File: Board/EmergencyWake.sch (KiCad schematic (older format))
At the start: 129 parts, among them J1 USB_C_Receptacle_USB2.0, J2 Micro_SD_Card_Det, J3 Conn_01x03, J4 Conn_01x02, J5 Conn_01x03, J6 Conn_01x04, J7 Conn_01x02, J8 Conn_01x04, J9 Conn_01x04, Q1 AO3400A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

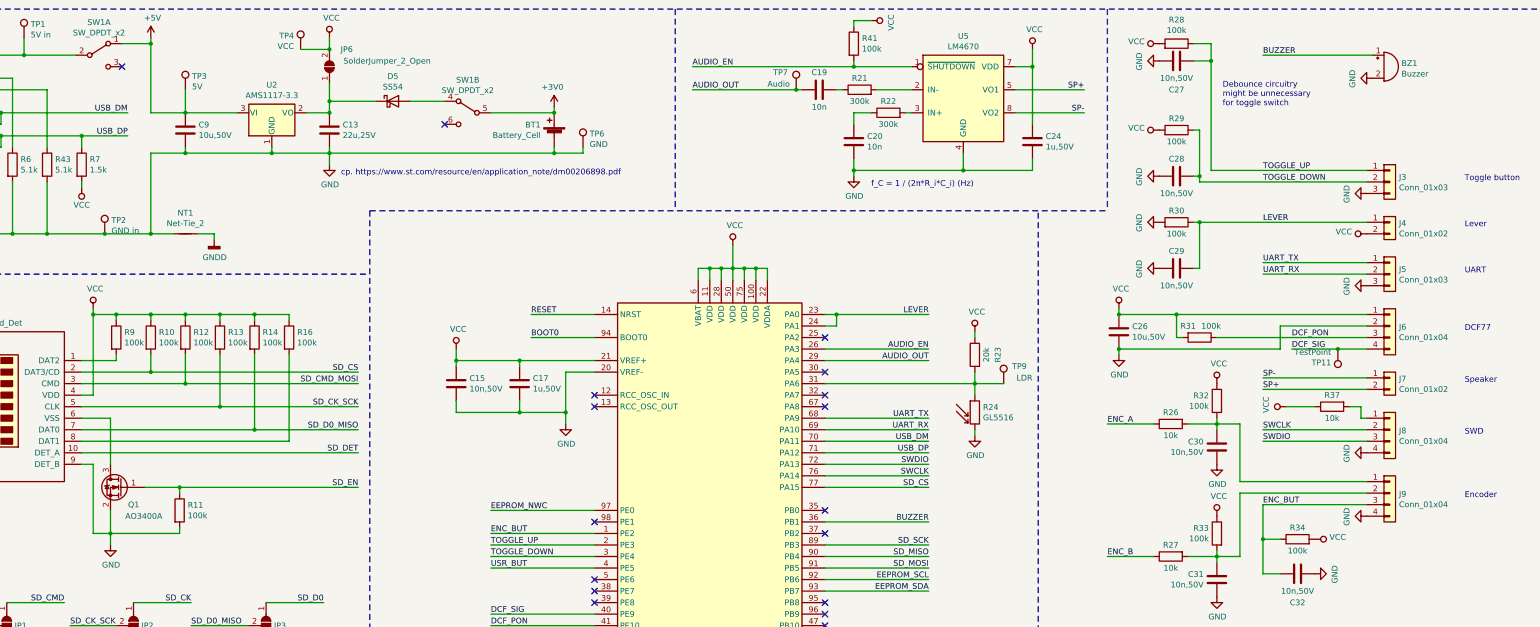
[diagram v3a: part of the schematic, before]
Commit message: [Board] Changed SD and battery holder to Würth components
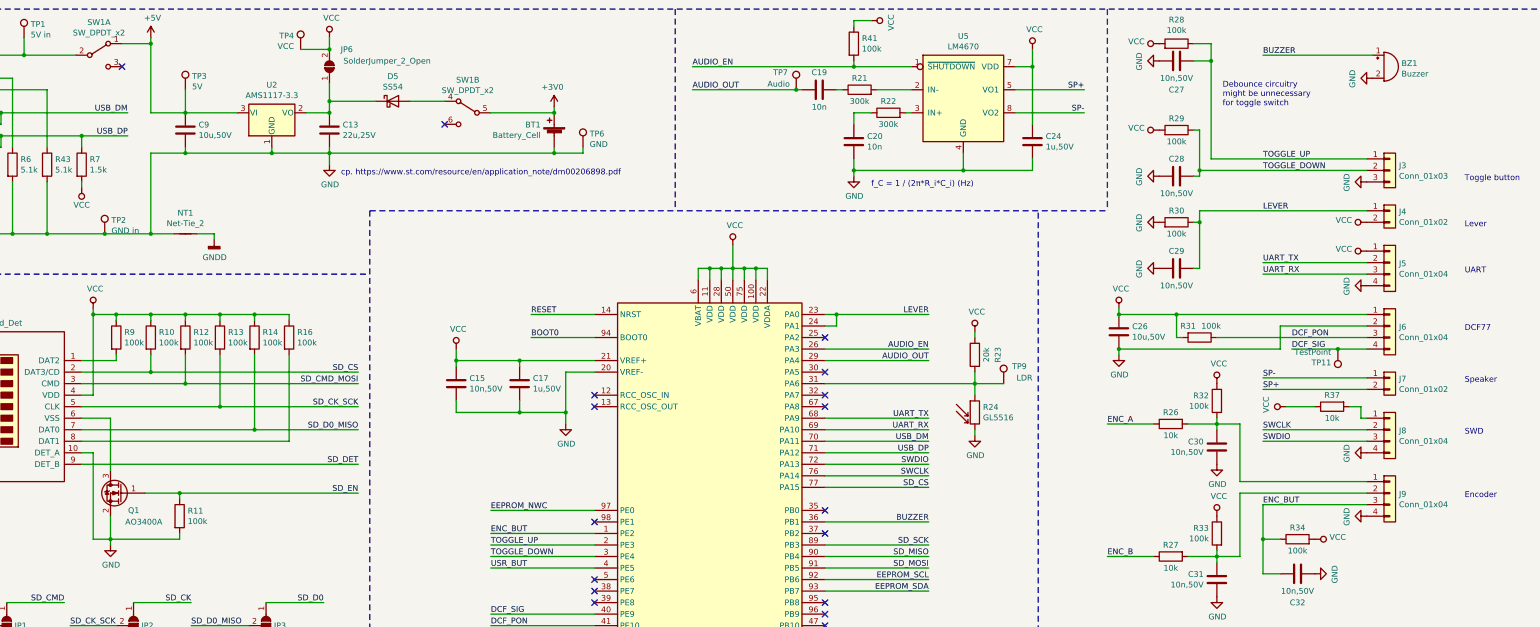
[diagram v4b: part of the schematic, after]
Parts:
- removed J5: Conn_01x03, Connector_PinHeader_2.54mm:PinHeader_1x03_P2.54mm_Horizontal, symbol Connector_Generic:Conn_01x03
- added J5: Conn_01x04, Connector_PinHeader_2.54mm:PinHeader_1x04_P2.54mm_Horizontal, symbol Connector_Generic:Conn_01x04
- BT1: footprint Battery:BatteryHolder_Keystone_3002_1x2032 -> Wuerth:79523141; Conrad 1009388 - 62 -> (none); Würth (none) -> 79523141
- J1: Würth (none) -> 632723300011
- J2: footprint Card:microSD_Attend_112I-TDAR-R 1 -> Wuerth:693071020811; Conrad 1308329 - 62 -> (none); Würth (none) -> 693071020811
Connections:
- net GND: now also J2.10 (DET_A), J5.4 (Pin_4); no longer J2.9 (DET_B)
- net SD_DET: now also J2.9 (DET_B); no longer J2.10 (DET_A)
- net UART_RX: now also J5.3 (Pin_3)
- net UART_TX: now also J5.2 (Pin_2)
- net VCC: now also J5.1 (Pin_1)
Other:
- moved on the sheet: J3, J4, Q1, R11
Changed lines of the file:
@@
 L Connector_Generic:Conn_01x02 J4
 U 1 1 5E2B13EE
-P 13900 2400
-F 0 "J4" H 13980 2392 50  0000 L CNN
-F 1 "Conn_01x02" H 13980 2301 50  0000 L CNN
-F 2 "Connector_PinHeader_2.54mm:PinHeader_1x02_P2.54mm_Horizontal" H 13900 2400 50  0001 C CNN
-F 3 "~" H 13900 2400 50  0001 C CNN
-	1    13900 2400
+P 13900 2300
+F 0 "J4" H 13980 2292 50  0000 L CNN
+F 1 "Conn_01x02" H 13980 2201 50  0000 L CNN
+F 2 "Connector_PinHeader_2.54mm:PinHeader_1x02_P2.54mm_Horizontal" H 13900 2300 50  0001 C CNN
+F 3 "~" H 13900 2300 50  0001 C CNN
+	1    13900 2300
 	1    0    0    -1
 $EndComp
@@
 F 0 "J2" H 1600 4817 50  0000 C CNN
 F 1 "Micro_SD_Card_Det" H 1600 4726 50  0000 C CNN
-F 2 "Card:microSD_Attend_112I-TDAR-R 1" H 3700 4700 50  0001 C CNN
-F 3 "https://asset.conrad.com/media10/add/160267/c1/-/en/001308329DS01/datenblatt-1308329-attend-microsd-kartensockel-druck-druck-112i-tdar-r-1-st.pdf" H 1650 4100 50  0001 C CNN
-F 4 "1308329 - 62" H 1650 4000 50  0001 C CNN "Conrad"
+F 2 "Wuerth:693071020811" H 3700 4700 50  0001 C CNN
+F 3 "https://www.we-online.de/katalog/datasheet/693071020811.pdf" H 1650 4100 50  0001 C CNN
+F 4 "693071020811" H 1650 4000 50  0001 C CNN "Würth"
 	1    1650 4000
 	-1   0    0    -1
@@
 F 0 "BT1" H 6768 1746 50  0000 L CNN
 F 1 "Battery_Cell" H 6768 1655 50  0000 L CNN
-F 2 "Battery:BatteryHolder_Keystone_3002_1x2032" V 6650 1710 50  0001 C CNN
-F 3 "https://www.conrad.de/de/p/renata-100340-knopfzellenhalter-1x-cr-2032-horizontal-oberflaechenmontage-smd-l-x-b-x-h-30-7-x-20-x-4-mm-1009388.html" V 6650 1710 50  0001 C CNN
-F 4 "1009388 - 62" H 6650 1650 50  0001 C CNN "Conrad"
+F 2 "Wuerth:79523141" V 6650 1710 50  0001 C CNN
+F 3 "https://www.we-online.de/katalog/datasheet/79523141.pdf" V 6650 1710 50  0001 C CNN
+F 4 "79523141" H 6650 1650 50  0001 C CNN "Würth"
 	1    6650 1650
 	-1   0    0    -1
@@
 	6650 1450 6100 1450
 Connection ~ 6650 1450
-$Comp
-L Connector_Generic:Conn_01x03 J5
-U 1 1 5E2E2ED5
-P 13900 2850
-F 0 "J5" H 13980 2892 50  0000 L CNN
-F 1 "Conn_01x03" H 13980 2801 50  0000 L CNN
-F 2 "Connector_PinHeader_2.54mm:PinHeader_1x03_P2.54mm_Horizontal" H 13900 2850 50  0001 C CNN
-F 3 "~" H 13900 2850 50  0001 C CNN
-	1    13900 2850
-	1    0    0    -1
-$EndComp
 Text Notes 14550 2850 0    50   ~ 0
 UART
@@
 L Device:Q_NMOS_GSD Q1
 U 1 1 5E31A1D8
-P 2900 4700
-F 0 "Q1" H 2750 4550 50  0000 L CNN
-F 1 "AO3400A" H 2550 4450 50  0000 L CNN
-F 2 "Package_TO_SOT_SMD:SOT-23" H 3100 4800 50  0001 C CNN
-F 3 "https://datasheet.lcsc.com/szlcsc/Alpha-Omega-Semicon-AOS-AO3400A_C20917.pdf" H 2900 4700 50  0001 C CNN
-F 4 "C20917" H 2900 4700 50  0001 C CNN "LCSC"
-	1    2900 4700
+P 2900 4750
+F 0 "Q1" H 2750 4600 50  0000 L CNN
+F 1 "AO3400A" H 2550 4500 50  0000 L CNN
+F 2 "Package_TO_SOT_SMD:SOT-23" H 3100 4850 50  0001 C CNN
+F 3 "https://datasheet.lcsc.com/szlcsc/Alpha-Omega-Semicon-AOS-AO3400A_C20917.pdf" H 2900 4750 50  0001 C CNN
+F 4 "C20917" H 2900 4750 50  0001 C CNN "LCSC"
+	1    2900 4750
 	-1   0    0    -1
 $EndComp
@@
 	2550 4100 2800 4100
 Wire Wire Line
-	2800 4100 2800 4500
+	2800 4100 2800 4550
 Wire Wire Line
-	2800 4900 2800 5100
+	2800 4950 2800 5150
 Wire Wire Line
-	2650 5100 2800 5100
-Connection ~ 2800 5100
+	2650 5150 2800 5150
+Connection ~ 2800 5150
 Wire Wire Line
-	2800 5100 2800 5200
+	2800 5150 2800 5200
 Wire Wire Line
 	2550 3900 2650 3900
@@
 $EndComp
 Wire Wire Line
-	3100 4700 3400 4700
+	3100 4750 3400 4750
 $Comp
 L power:GND #PWR03
@@
 $EndComp
 Wire Wire Line
-	2800 5100 3400 5100
+	2800 5150 3400 5150
 Wire Wire Line
-	3400 5100 3400 5050
+	3400 5150 3400 5100
 Wire Wire Line
-	3400 4750 3400 4700
-Connection ~ 3400 4700
+	3400 4800 3400 4750
+Connection ~ 3400 4750
 Wire Wire Line
-	3400 4700 4950 4700
-Text Label 4950 4700 2    50   ~ 0
+	3400 4750 4950 4750
+Text Label 4950 4750 2    50   ~ 0
 SD_EN
-Text Label 4950 4400 2    50   ~ 0
+Text Label 4950 4500 2    50   ~ 0
 SD_DET
 $Comp
@@
 L Device:R R11
 U 1 1 5E33508E
-P 3400 4900
-F 0 "R11" H 3470 4946 50  0000 L CNN
-F 1 "100k" H 3470 4855 50  0000 L CNN
-F 2 "Resistor_SMD:R_0402_1005Metric" V 3330 4900 50  0001 C CNN
-F 3 "~" H 3400 4900 50  0001 C CNN
-F 4 "C25741" H 3400 4900 50  0001 C CNN "LCSC"
-	1    3400 4900
+P 3400 4950
+F 0 "R11" H 3470 4996 50  0000 L CNN
+F 1 "100k" H 3470 4905 50  0000 L CNN
+F 2 "Resistor_SMD:R_0402_1005Metric" V 3330 4950 50  0001 C CNN
+F 3 "~" H 3400 4950 50  0001 C CNN
+F 4 "C25741" H 3400 4950 50  0001 C CNN "LCSC"
+	1    3400 4950
 	1    0    0    -1
 $EndComp
@@
 Text Label 13050 3500 0    50   ~ 0
 DCF_SIG
-Text Label 12800 1950 0    50   ~ 0
+Text Label 12800 1850 0    50   ~ 0
 TOGGLE_UP
-Text Label 12800 2050 0    50   ~ 0
+Text Label 12800 1950 0    50   ~ 0
 TOGGLE_DOWN
-Text Label 12800 2400 0    50   ~ 0
+Text Label 12800 2300 0    50   ~ 0
 LEVER
 Text Label 11450 4150 0    50   ~ 0
@@
 $EndComp
 Wire Wire Line
-	12200 2400 12250 2400
-Wire Wire Line
 	12200 2800 12250 2800
 Wire Wire Line
 	12250 2800 12250 2400
-Connection ~ 12250 2400
 Wire Wire Line
-	12250 2400 13700 2400
+	12250 2300 13700 2300
 Wire Wire Line
-	12250 2050 12250 2000
+	12250 1950 12250 2000
 Wire Wire Line
 	12250 2000 12200 2000
@@
 	12200 1600 12250 1600
 Wire Wire Line
-	12250 1600 12250 2000
-Connection ~ 12250 2000
+	12250 1600 12250 1950
 Wire Wire Line
-	12350 1950 12350 1000
+	12350 1850 12350 1000
 Wire Wire Line
 	12350 1000 12200 1000
@@
 $EndComp
 $Comp
-L Connector:TestPoint TP1
-U 1 1 5E3C768F
-P 2050 800
-F 0 "TP1" H 2108 918 50  0000 L CNN
-F 1 "5V in" H 2108 827 50  0000 L CNN
-F 2 "TestPoint:TestPoint_Loop_D1.80mm_Drill1.0mm_Beaded" H 2250 800 50  0001 C CNN
-F 3 "~" H 2250 800 50  0001 C CNN
-	1    2050 800
-	1    0    0    -1
-$EndComp
-$Comp
 L Connector:TestPoint TP2
 U 1 1 5E3C8161
@@
 	5050 2300 11450 2300
 Wire Wire Line
-	12250 2050 13700 2050
+	12250 1950 13700 1950
 Wire Wire Line
-	12350 1950 13700 1950
+	12350 1850 13700 1850
 $Comp
 L Connector_Generic:Conn_01x03 J3
 U 1 1 5E2B1093
-P 13900 2050
-F 0 "J3" H 13980 2092 50  0000 L CNN
-F 1 "Conn_01x03" H 13980 2001 50  0000 L CNN
-F 2 "Connector_PinHeader_2.54mm:PinHeader_1x03_P2.54mm_Horizontal" H 13900 2050 50  0001 C CNN
-F 3 "~" H 13900 2050 50  0001 C CNN
-	1    13900 2050
+P 13900 1950
+F 0 "J3" H 13980 1992 50  0000 L CNN
+F 1 "Conn_01x03" H 13980 1901 50  0000 L CNN
+F 2 "Connector_PinHeader_2.54mm:PinHeader_1x03_P2.54mm_Horizontal" H 13900 1950 50  0001 C CNN
+F 3 "~" H 13900 1950 50  0001 C CNN
+	1    13900 1950
 	1    0    0    -1
 $EndComp
@@
 L power:VCC #PWR048
 U 1 1 5E63717C
-P 13700 2500
-F 0 "#PWR048" H 13700 2350 50  0001 C CNN
-F 1 "VCC" V 13718 2627 50  0000 L CNN
-F 2 "" H 13700 2500 50  0001 C CNN
-F 3 "" H 13700 2500 50  0001 C CNN
-	1    13700 2500
+P 13700 2400
+F 0 "#PWR048" H 13700 2250 50  0001 C CNN
+F 1 "VCC" V 13718 2527 50  0000 L CNN
+F 2 "" H 13700 2400 50  0001 C CNN
+F 3 "" H 13700 2400 50  0001 C CNN
+	1    13700 2400
 	0    -1   -1   0
 $EndComp
@@
 L power:GND #PWR059
 U 1 1 5E40A111
-P 13700 2150
-F 0 "#PWR059" H 13700 1900 50  0001 C CNN
-F 1 "GND" H 13705 1977 50  0000 C CNN
-F 2 "" H 13700 2150 50  0001 C CNN
-F 3 "" H 13700 2150 50  0001 C CNN
-	1    13700 2150
+P 13700 2050
+F 0 "#PWR059" H 13700 1800 50  0001 C CNN
+F 1 "GND" H 13705 1877 50  0000 C CNN
+F 2 "" H 13700 2050 50  0001 C CNN
+F 3 "" H 13700 2050 50  0001 C CNN
+	1    13700 2050
 	0    1    1    0
 $EndComp
@@
 Wire Wire Line
 	9250 1950 10200 1950
-Wire Wire Line
-	2550 4500 2650 4500
-Wire Wire Line
-	2650 4500 2650 5100
-Wire Wire Line
-	4950 4400 2550 4400
 $Comp
 L Connector:USB_C_Receptacle_USB2.0 J1
@@
 F 2 "Wuerth:632723300011" H 1350 1550 50  0001 C CNN
 F 3 "https://www.usb.org/sites/default/files/documents/usb_type-c.zip" H 1350 1550 50  0001 C CNN
+F 4 "632723300011" H 1200 1550 50  0001 C CNN "Würth"
 	1    1200 1550
 	1    0    0    -1
@@
 	4450 900  4700 900
 Connection ~ 4700 900
+$Comp
+L Connector:TestPoint TP1
+U 1 1 5E3C768F
+P 2050 800
+F 0 "TP1" H 2108 918 50  0000 L CNN
+F 1 "5V in" H 2108 827 50  0000 L CNN
+F 2 "TestPoint:TestPoint_Loop_D1.80mm_Drill1.0mm_Beaded" H 2250 800 50  0001 C CNN
+F 3 "~" H 2250 800 50  0001 C CNN
+	1    2050 800
+	1    0    0    -1
+$EndComp
+Wire Wire Line
+	2650 4400 2550 4400
+Wire Wire Line
+	2650 4400 2650 5150
+Wire Wire Line
+	2550 4500 4950 4500
+$Comp
+L Connector_Generic:Conn_01x04 J5
+U 1 1 5E97C9A1
+P 13900 2750
+F 0 "J5" H 13980 2742 50  0000 L CNN
+F 1 "Conn_01x04" H 13980 2651 50  0000 L CNN
+F 2 "Connector_PinHeader_2.54mm:PinHeader_1x04_P2.54mm_Horizontal" H 13900 2750 50  0001 C CNN
+F 3 "~" H 13900 2750 50  0001 C CNN
+	1    13900 2750
+	1    0    0    -1
+$EndComp
+$Comp
+L power:VCC #PWR0102
+U 1 1 5E97D3B4
+P 13700 2650
+F 0 "#PWR0102" H 13700 2500 50  0001 C CNN
+F 1 "VCC" V 13718 2777 50  0000 L CNN
+F 2 "" H 13700 2650 50  0001 C CNN
+F 3 "" H 13700 2650 50  0001 C CNN
+	1    13700 2650
+	0    -1   -1   0
+$EndComp
+Connection ~ 12250 1950
+Wire Wire Line
+	12200 2400 12250 2400
+Connection ~ 12250 2400
+Wire Wire Line
+	12250 2400 12250 2300
 $EndSCHEMATC
